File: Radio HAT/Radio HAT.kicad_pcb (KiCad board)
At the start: 2 copper layers, 65 x 45 mm, 26 parts, among them J1 Raspberry_Pi_2_3, J2 Coax SMA, J3 Barrel_Jack, J4 VCC, J5 6V, J6 GND, U1 RFM98PW, U2 AZ2185D-ADJTRG1

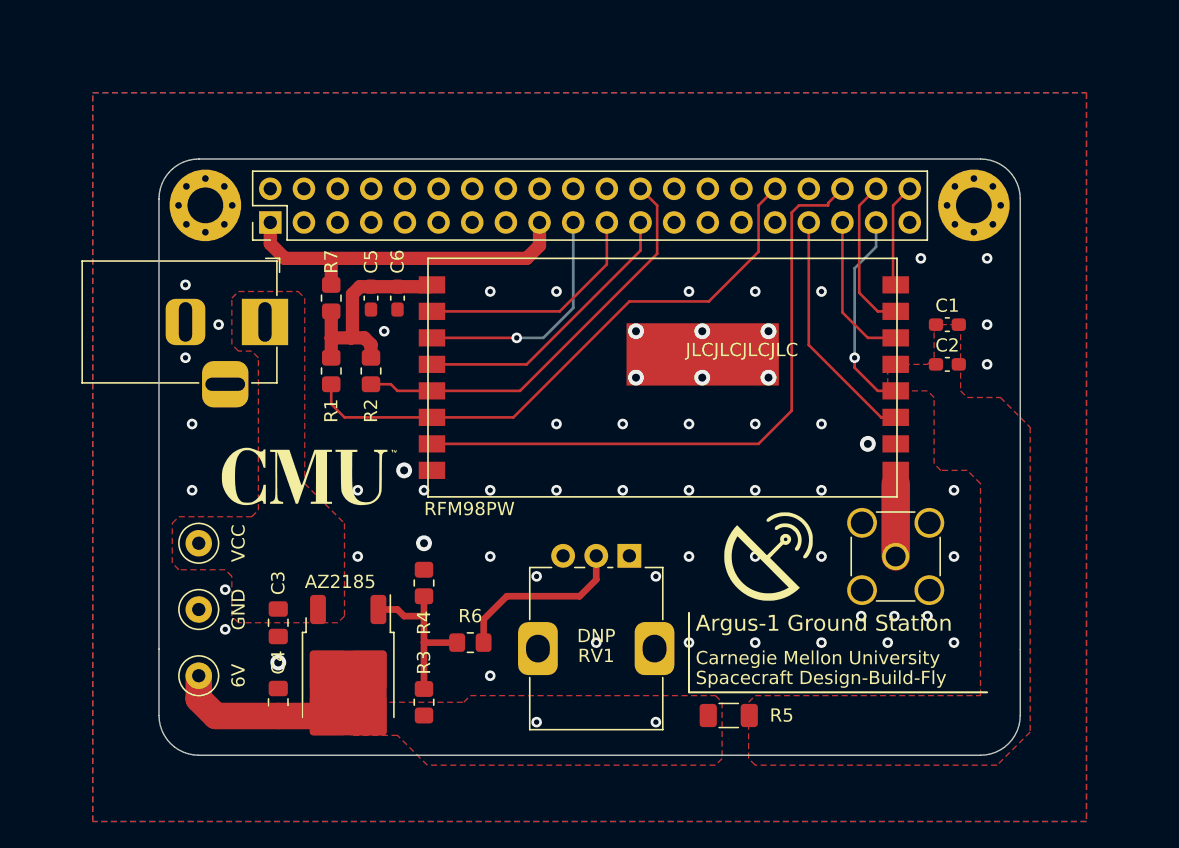
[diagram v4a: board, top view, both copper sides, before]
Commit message: Updated copper pours
Copper pours had gone out of alignment, reworked and increased sizes
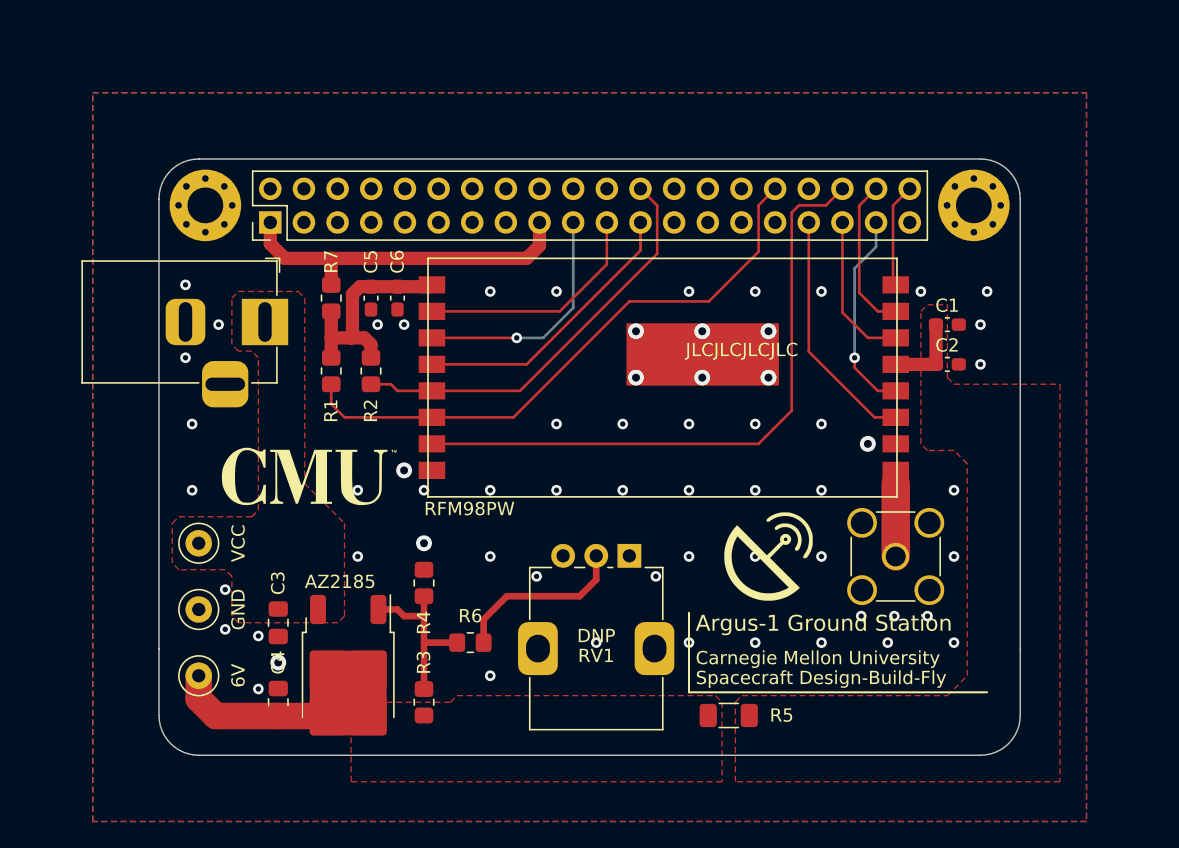
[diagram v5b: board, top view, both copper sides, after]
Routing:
- net /V_RF: track 0.00 -> 6.04 mm
- net GND: vias 59 -> 62
- net +6V: vias 2 -> 0
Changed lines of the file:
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@@
   (title_block
     (title "Argus-1 Ground Station")
-    (date "2023-10-29")
+    (date "2023-10-30")
     (rev "v1.1")
     (company "Carnegie Mellon University")
@@
   (segment (start 112.6925 142.0375) (end 112.755 141.975) (width 2) (layer "F.Cu") (net 1))
   (segment (start 109 142.0375) (end 112.6925 142.0375) (width 2) (layer "F.Cu") (net 1))
-  (via (at 137.5 142.5) (size 0.8) (drill 0.4) (layers "F.Cu" "B.Cu") (free) (net 1))
-  (via (at 128.5 142.5) (size 0.8) (drill 0.4) (layers "F.Cu" "B.Cu") (free) (net 1))
   (via (at 145 110) (size 0.8) (drill 0.4) (layers "F.Cu" "B.Cu") (free) (net 2))
+  (via (at 157.5 110) (size 0.8) (drill 0.4) (layers "F.Cu" "B.Cu") (free) (net 2))
   (via (at 145 120) (size 0.8) (drill 0.4) (layers "F.Cu" "B.Cu") (free) (net 2))
   (via (at 136 113) (size 1.2) (drill 0.6) (layers "F.Cu" "B.Cu") (net 2))
@@
   (via (at 135 125) (size 0.8) (drill 0.4) (layers "F.Cu" "B.Cu") (free) (net 2))
   (via (at 140 120) (size 0.8) (drill 0.4) (layers "F.Cu" "B.Cu") (free) (net 2))
-  (via (at 162.5 115.5) (size 0.8) (drill 0.4) (layers "F.Cu" "B.Cu") (free) (net 2))
+  (via (at 162 115.5) (size 0.8) (drill 0.4) (layers "F.Cu" "B.Cu") (free) (net 2))
+  (via (at 116.5 112.5) (size 0.8) (drill 0.4) (layers "F.Cu" "B.Cu") (free) (net 2))
   (via (at 130 110) (size 0.8) (drill 0.4) (layers "F.Cu" "B.Cu") (free) (net 2))
   (via (at 118.5 123.5) (size 1.2) (drill 0.6) (layers "F.Cu" "B.Cu") (free) (net 2))
-  (via (at 117 113) (size 0.8) (drill 0.4) (layers "F.Cu" "B.Cu") (free) (net 2))
+  (via (at 162.5 110) (size 0.8) (drill 0.4) (layers "F.Cu" "B.Cu") (free) (net 2))
+  (via (at 118.5 112.5) (size 0.8) (drill 0.4) (layers "F.Cu" "B.Cu") (free) (net 2))
   (via (at 115 125) (size 0.8) (drill 0.4) (layers "F.Cu" "B.Cu") (free) (net 2))
-  (via (at 162.5 107.5) (size 0.8) (drill 0.4) (layers "F.Cu" "B.Cu") (free) (net 2))
+  (via (at 107.5 136) (size 0.8) (drill 0.4) (layers "F.Cu" "B.Cu") (free) (net 2))
   (via (at 137.5 131.5) (size 0.8) (drill 0.4) (layers "F.Cu" "B.Cu") (free) (net 2))
   (via (at 150 130) (size 0.8) (drill 0.4) (layers "F.Cu" "B.Cu") (free) (net 2))
@@
   (via (at 128.5 131.5) (size 0.8) (drill 0.4) (layers "F.Cu" "B.Cu") (free) (net 2))
   (via (at 125 130) (size 0.8) (drill 0.4) (layers "F.Cu" "B.Cu") (free) (net 2))
-  (via (at 162.5 112.5) (size 0.8) (drill 0.4) (layers "F.Cu" "B.Cu") (free) (net 2))
+  (via (at 162 112.5) (size 0.8) (drill 0.4) (layers "F.Cu" "B.Cu") (free) (net 2))
   (via (at 102 109.5) (size 0.8) (drill 0.4) (layers "F.Cu" "B.Cu") (free) (net 2))
   (via (at 130 125) (size 0.8) (drill 0.4) (layers "F.Cu" "B.Cu") (free) (net 2))
@@
   (via (at 105 135.5) (size 0.8) (drill 0.4) (layers "F.Cu" "B.Cu") (free) (net 2))
   (via (at 120 129) (size 1.2) (drill 0.6) (layers "F.Cu" "B.Cu") (free) (net 2))
+  (via (at 107.5 140) (size 0.8) (drill 0.4) (layers "F.Cu" "B.Cu") (free) (net 2))
   (via (at 102.5 125) (size 0.8) (drill 0.4) (layers "F.Cu" "B.Cu") (free) (net 2))
   (via (at 155.5 134.5) (size 0.8) (drill 0.4) (layers "F.Cu" "B.Cu") (free) (net 2))
@@
   (via (at 120 125) (size 0.8) (drill 0.4) (layers "F.Cu" "B.Cu") (free) (net 2))
   (via (at 140 125) (size 0.8) (drill 0.4) (layers "F.Cu" "B.Cu") (free) (net 2))
-  (via (at 157.5 107.5) (size 0.8) (drill 0.4) (layers "F.Cu" "B.Cu") (free) (net 2))
   (via (at 104.5 112.5) (size 0.8) (drill 0.4) (layers "F.Cu" "B.Cu") (free) (net 2))
   (via (at 145 125) (size 0.8) (drill 0.4) (layers "F.Cu" "B.Cu") (free) (net 2))
@@
   (segment (start 128.72 106.53) (end 127.75 107.5) (width 1) (layer "F.Cu") (net 4))
   (segment (start 108.4 106.4) (end 108.4 104.79) (width 1) (layer "F.Cu") (net 4))
-  (segment (start 150.5 103.5) (end 150.5 103.33) (width 0.2) (layer "F.Cu") (net 13))
-  (segment (start 150.5 103.33) (end 151.58 102.25) (width 0.2) (layer "F.Cu") (net 13))
   (segment (start 145.25 121.5) (end 147.75 119) (width 0.2) (layer "F.Cu") (net 13))
+  (segment (start 147.75 119) (end 147.75 104.05) (width 0.2) (layer "F.Cu") (net 13))
+  (segment (start 120.6 121.5) (end 145.25 121.5) (width 0.2) (layer "F.Cu") (net 13))
+  (segment (start 150.33 103.5) (end 151.58 102.25) (width 0.2) (layer "F.Cu") (net 13))
+  (segment (start 148.3 103.5) (end 150.33 103.5) (width 0.2) (layer "F.Cu") (net 13))
   (segment (start 147.75 104.05) (end 148.3 103.5) (width 0.2) (layer "F.Cu") (net 13))
-  (segment (start 147.75 119) (end 147.75 104.05) (width 0.2) (layer "F.Cu") (net 13))
-  (segment (start 148.3 103.5) (end 150.5 103.5) (width 0.2) (layer "F.Cu") (net 13))
-  (segment (start 120.6 121.5) (end 145.25 121.5) (width 0.2) (layer "F.Cu") (net 13))
   (segment (start 153.5 113.5) (end 151.58 111.58) (width 0.2) (layer "F.Cu") (net 14))
   (segment (start 155.6 113.5) (end 153.5 113.5) (width 0.2) (layer "F.Cu") (net 14))
@@
   (segment (start 133.8 107.95) (end 133.8 104.79) (width 0.2) (layer "F.Cu") (net 18))
   (segment (start 130.25 111.5) (end 133.8 107.95) (width 0.2) (layer "F.Cu") (net 18))
-  (segment (start 155.6 119.5) (end 154.5 119.5) (width 0.2) (layer "F.Cu") (net 19))
-  (segment (start 149.04 114.04) (end 149.04 104.79) (width 0.2) (layer "F.Cu") (net 19))
-  (segment (start 154.5 119.5) (end 149.04 114.04) (width 0.2) (layer "F.Cu") (net 19))
+  (segment (start 155.6 119.5) (end 154 119.5) (width 0.2) (layer "F.Cu") (net 19))
+  (segment (start 149.04 114.54) (end 149.04 104.79) (width 0.2) (layer "F.Cu") (net 19))
+  (segment (start 154 119.5) (end 149.04 114.54) (width 0.2) (layer "F.Cu") (net 19))
   (segment (start 120.6 115.5) (end 127.75 115.5) (width 0.2) (layer "F.Cu") (net 20))
   (segment (start 136.34 106.91) (end 136.34 104.79) (width 0.2) (layer "F.Cu") (net 20))
@@
   (segment (start 133 131.75) (end 133 129.95) (width 0.5) (layer "F.Cu") (net 38))
   (segment (start 126.25 133) (end 131.75 133) (width 0.5) (layer "F.Cu") (net 38))
+  (segment (start 155.6 115.5) (end 158.6375 115.5) (width 1) (layer "F.Cu") (net 40))
+  (segment (start 158.6375 115.5) (end 158.6375 112.5) (width 1) (layer "F.Cu") (net 40))
+  (zone (net 1) (net_name "+6V") (layer "F.Cu") (hatch edge 0.5)
+    (priority 1)
+    (connect_pads (clearance 0.5))
+    (min_thickness 0.25) (filled_areas_thickness no)
+    (fill yes (thermal_gap 0.5) (thermal_bridge_width 0.5))
+    (polygon
+      (pts
+        (xy 122 141)
+        (xy 122.5 140.5)
+        (xy 142 140.5)
+        (xy 142.5 141)
+        (xy 142.5 147)
+        (xy 114.5 147)
+        (xy 114.5 141.5)
+        (xy 115 141)
+      )
+    )
+  )
   (zone (net 40) (net_name "/V_RF") (layer "F.Cu") (hatch edge 0.5)
     (priority 1)
@@
     (polygon
       (pts
-        (xy 144.5 141)
-        (xy 145 140.5)
-        (xy 162 140.5)
-        (xy 162 124.5)
-        (xy 161 123.5)
-        (xy 159 123.5)
-        (xy 158.5 123)
-        (xy 158.5 118)
-        (xy 158 117.5)
-        (xy 155.5 117.5)
-        (xy 155 117)
-        (xy 155 116)
-        (xy 155.5 115.5)
-        (xy 158 115.5)
-        (xy 158.5 115)
-        (xy 158.5 113)
-        (xy 159 112.5)
-        (xy 160.5 112.5)
-        (xy 160.5 117.5)
-        (xy 161 118)
-        (xy 163.5 118)
-        (xy 165.75 120.25)
-        (xy 165.75 143.25)
-        (xy 163.25 145.75)
-        (xy 145 145.75)
-        (xy 144.5 145.25)
+        (xy 143.5 141)
+        (xy 144 140.5)
+        (xy 159.5 140.5)
+        (xy 161 139)
+        (xy 161 123)
+        (xy 160 122)
+        (xy 158 122)
+        (xy 157.5 121.5)
+        (xy 157.5 111.5)
+        (xy 158 111)
+        (xy 159.5 111)
+        (xy 159.5 116.5)
+        (xy 160 117)
+        (xy 168 117)
+        (xy 168 147)
+        (xy 143.5 147)
       )
     )
-  )
-  (zone (net 1) (net_name "+6V") (layer "F.Cu") (hatch edge 0.5)
-    (priority 1)
-    (connect_pads (clearance 0.5))
-    (min_thickness 0.25) (filled_areas_thickness no)
-    (fill yes (thermal_gap 0.5) (thermal_bridge_width 0.5))
-    (polygon
-      (pts
-        (xy 123 141)
-        (xy 123.5 140.5)
-        (xy 142 140.5)
-        (xy 142.5 141)
-        (xy 142.5 145.25)
-        (xy 142 145.75)
-        (xy 120.25 145.75)
-        (xy 118 143.5)
-        (xy 114.5 143.5)
-        (xy 114.5 141)
-      )
-    )

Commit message: Converted to 4-layer board
Changes:
- added 2 internal layers
- stackup: PWR - GND - SIG - GND
- added POW indicator LED
- increased density of stitching vias
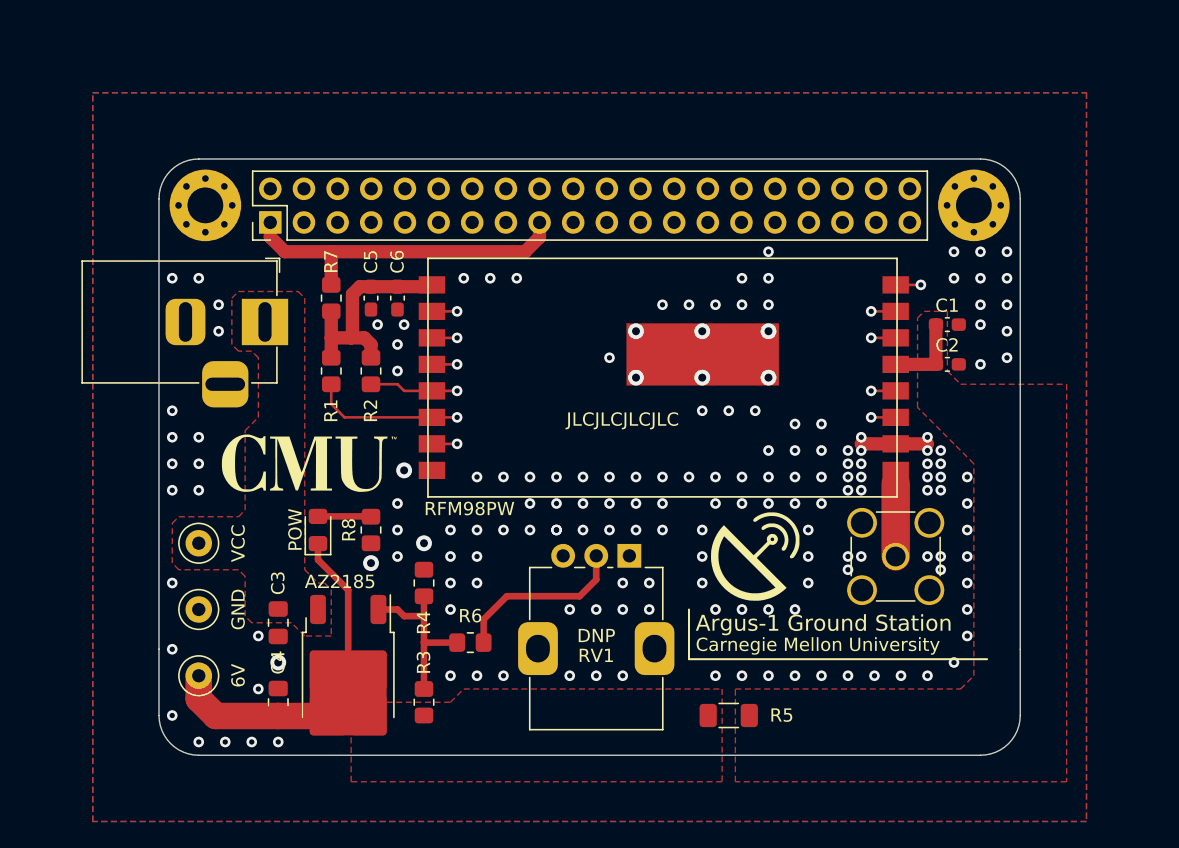
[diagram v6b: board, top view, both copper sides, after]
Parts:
- added D1: POW, LED_SMD:LED_0805_2012Metric_Pad1.15x1.40mm_HandSolder, F.Cu at (112.0, 128.0)
- added R8: 200, Resistor_SMD:R_0805_2012Metric_Pad1.20x1.40mm_HandSolder, F.Cu at (116.0, 128.0)
- moved G*** 1.00 mm to (111.0, 123.0)
- moved G*** 1.00 mm to (145.0, 130.0)
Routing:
- net +6V: track 12.1 -> 24.3 mm
- net /RF_DIO4: track 15.5 -> 21.6 mm
- net GND: track 0.00 -> 5.00 mm, vias 62 -> 172
- net Net-(D1-A): track 0.00 -> 4.01 mm
- net /RF_MISO: track 17.8 -> 20.6 mm, vias 0 -> 1
- net /RF_DIO2: track 7.85 -> 9.91 mm, vias 0 -> 1
- net /RF_DIO1: track 11.7 -> 12.7 mm, vias 0 -> 1
- net /RF_MOSI: track 18.0 -> 17.2 mm
- net /RF_DIO3: track 18.4 -> 19.2 mm, vias 0 -> 1
- net /RF_DIO5: track 47.7 -> 47.0 mm, vias 0 -> 1
- net /RPI_3V3: track 26.5 -> 26.0 mm
- net /RF_RESET: track 44.6 -> 44.2 mm, vias 0 -> 1
- net /RF_SCK: track 21.4 -> 21.3 mm, vias 0 -> 1
- net /RF_CS: track 31.5 -> 31.7 mm, vias 0 -> 1
- net /RF_DIO0: track 11.6 -> 11.5 mm, vias 0 -> 1
- added copper zone on In1.Cu, net GND
- added copper zone on In2.Cu, net GND
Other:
- copper layers 2 -> 4
- board text added: "POW"
- board text removed: "Spacecraft Design-Build-Fly"

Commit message: Radio HAT v1.1 redesign
Changes:
- Board is back to PWR-GND-SIG-GND
- Made small electrical changes in a lot of spots with Jason
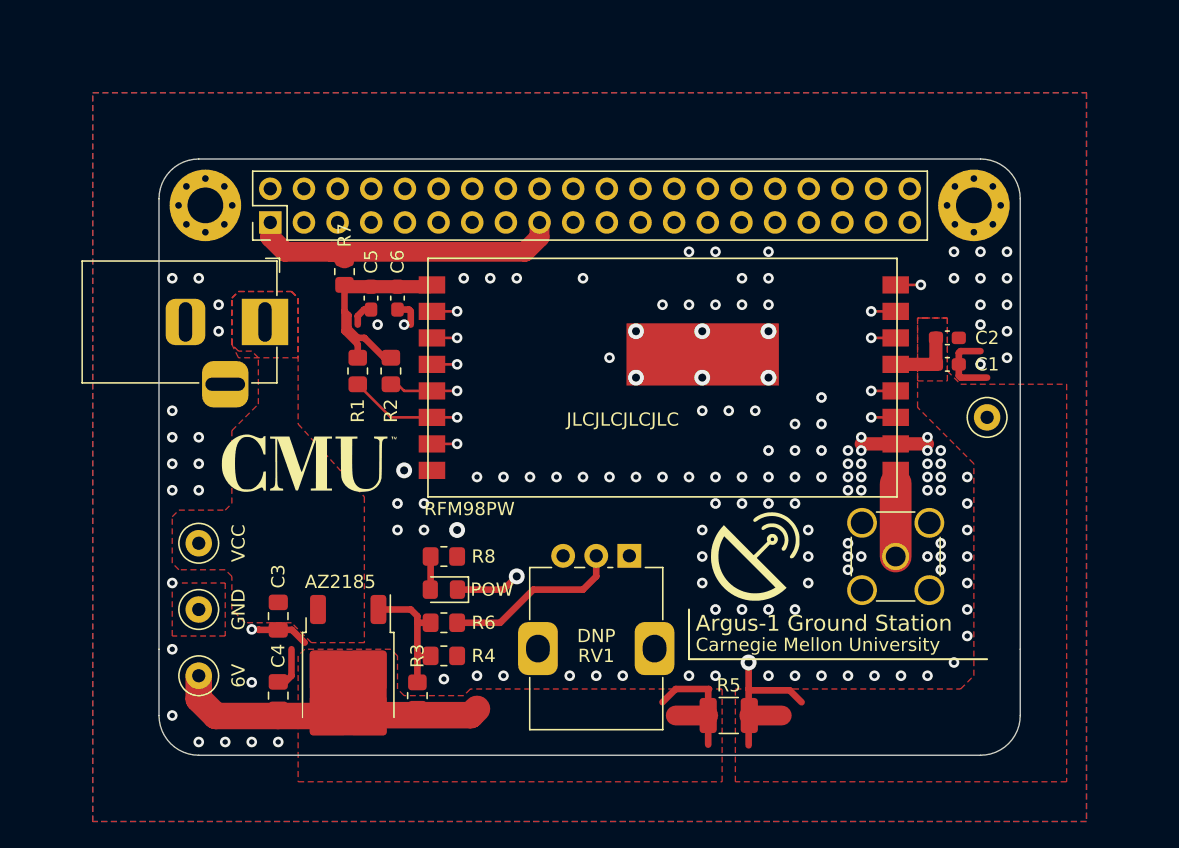
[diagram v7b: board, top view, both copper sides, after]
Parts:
- added J7: V_RF, TestPoint:TestPoint_Loop_D2.50mm_Drill1.0mm, F.Cu at (162.5, 119.5)
- R5: footprint Resistor_SMD:R_1206_3216Metric_Pad1.30x1.75mm_HandSolder -> Resistor_SMD:R_1210_3225Metric_Pad1.30x2.65mm_HandSolder
- moved D1 10.5 mm to (121.5, 132.5), turned to 180 degrees
- moved R8 5.85 mm to (121.5, 130.0), turned to 180 degrees
- moved R4 5.70 mm to (121.5, 137.5), turned to 0 degrees
- moved C1 3.00 mm to (159.5, 115.5)
- moved R6 2.50 mm to (121.5, 135.0)
- moved R7 2.24 mm to (114.0, 108.5)
- moved C2 2.00 mm to (159.5, 113.5)
- moved R1 2.00 mm to (115.0, 116.0)
- moved R2 1.50 mm to (117.5, 116.0)
- moved R3 0.71 mm to (119.5, 140.5)
- moved C3 0.50 mm to (109.0, 134.5)
- moved C4 0.50 mm to (109.0, 140.5)
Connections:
- D1 pad 1: +6V -> /V_RF
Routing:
- net /V_RF: track 6.04 -> 55.3 mm, vias 0 -> 2
- net GND: track 5.00 -> 21.6 mm, vias 172 -> 147
- net +6V: track 24.3 -> 34.1 mm
- net /REG_ADJ: track 13.1 -> 10.1 mm
- net /RF_RESET: track 44.2 -> 41.3 mm
- net Net-(D1-A): track 4.01 -> 2.51 mm
- net /RF_CS: track 31.7 -> 30.2 mm
- net /RPI_3V3: track 26.0 -> 24.7 mm
- net +3V3: track 17.3 -> 18.2 mm
